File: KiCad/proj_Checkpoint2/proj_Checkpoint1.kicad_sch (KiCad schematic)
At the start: 32 parts, among them M1 Motor_Servo, Q2 MOSFET-N, SW1 Reset, U1 74xxx244, U1 MCP6294, U1 PIC32MX170F256B, U2 Comparator, U5 SW_CapTouch, U8 LED_Matrix

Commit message: clean build
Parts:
- added D4, D5, D6: LED, symbol Device:LED
- added R10, R12: 10k, symbol ME218_BaseLib:Res1
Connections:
- net GNDREF: now also D4.1 (K), D5.1 (K), D6.1 (K); no longer R1.2
- net out: now also U1.17 (5VT/RB8), U1.18 (PGED2/5VT/RB9), U1.24 (RB13)
- net at RV1.2: now also U1.26 (RB15); no longer U1.11 (RB4)
- net at D3.1 (K): no longer D2.2 (A)
- net at D3.2 (A): no longer U1.9 (RA2)
- net at R1.1: now also U1.21 (PGEC2/5VT/RB10); no longer D2.1 (K)
- net at U1.22 (RB11): now also R10.1
- net at U1.23 (RB12): now also R12.1
- new net: D6.2 (A), R12.2
- new net: D4.2 (A), R1.2
- new net: D5.2 (A), R10.2

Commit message: kicad update
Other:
- note added: "Coin Detector IR"
- note added: "Goal Sensor IR"
- note added: "Miss Sensor"
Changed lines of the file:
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@@
+    (stroke (width 0) (type default))
+  )
+  (wire (pts (xy 80.01 121.92) (xy 78.74 121.92))
+    (stroke (width 0) (type default))
+  )
+  (wire (pts (xy 154.94 96.52) (xy 154.94 99.06))
+    (stroke (width 0) (type default))
+  )
+  (wire (pts (xy 132.08 110.49) (xy 140.97 110.49))
+    (stroke (width 0) (type default))
+  )
+  (wire (pts (xy 134.62 182.88) (xy 138.43 182.88))
     (stroke (width 0) (type default))
   )
   (wire (pts (xy 132.08 130.81) (xy 137.16 130.81))
-    (stroke (width 0) (type default))
-  )
-  (wire (pts (xy 80.01 121.92) (xy 78.74 121.92))
-    (stroke (width 0) (type default))
-  )
-  (wire (pts (xy 154.94 96.52) (xy 154.94 99.06))
-    (stroke (width 0) (type default))
-  )
-  (wire (pts (xy 132.08 110.49) (xy 140.97 110.49))
-    (stroke (width 0) (type default))
-  )
-  (wire (pts (xy 134.62 182.88) (xy 138.43 182.88))
     (stroke (width 0) (type default))
   )
@@
     (effects (font (size 1.27 1.27)) (justify left bottom))
   )
-  (text "IR Sensor Signal Regulator\n" (at 106.68 171.45 0)
+  (text "Coin Detector IR" (at 106.68 171.45 0)
     (effects (font (size 1.27 1.27)) (justify left bottom))
   )
-  (text "IR Sensor Signal Regulator\n" (at 106.68 189.23 0)
+  (text "Goal Sensor IR\n" (at 106.68 189.23 0)
     (effects (font (size 1.27 1.27)) (justify left bottom))
   )
@@
     (effects (font (size 1.27 1.27)) (justify left bottom))
   )
-  (text "IR Sensor Signal Regulator\n" (at 106.68 180.34 0)
+  (text "Miss Sensor" (at 106.68 180.34 0)
     (effects (font (size 1.27 1.27)) (justify left bottom))
   )

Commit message: Updated KiCAD for Checkpoint 2
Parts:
- removed D2: IR LED1, symbol ME218_BaseLib:LED
- removed D3: IR LED0, symbol ME218_BaseLib:LED
- removed IR_Sensor0, IR_Sensor1: Photo_NPN, symbol ME218_BaseLib:Photo_NPN
- removed R2, R3: 10k, symbol ME218_BaseLib:Res1
- removed R4, R5: 330k, symbol ME218_BaseLib:Res1
- removed R6, R7: 22k, symbol ME218_BaseLib:Res1
- removed R8: 100k, symbol ME218_BaseLib:Res1
- removed R_pull1: 3.3k, symbol ME218_BaseLib:Res1
- removed U1: MCP6294, symbol ME218_BaseLib:MCP6294
- removed U2: Comparator, symbol ME218_BaseLib:MCP6294
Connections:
- net out: no longer U1.4 (PGED1/RB0), U1.5 (PGEC1/RB1)
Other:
- note added: "Coin Detector IR Emitter-Detector"
- note added: "Goal Sensor IR Emitter-Detector"
- note added: "Miss Sensor IR Emitter-Detector"
- note removed: "Coin Detector IR"
- note removed: "Goal Sensor IR"
- note removed: "IR Sensor Signal Regulator"
- note removed: "IR Sensor0 Output"
- note removed: "IR Sensor1 Output"
- note removed: "Miss Sensor"
- note removed: "input"
- title: (none) -> Project Checkpoint 2
- moved on the sheet: C1, C2, C3, C4, M1, Q2, R_gate, SW1, U1, U5, U8

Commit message: kicad update for report
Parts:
- removed U5: SW_CapTouch, symbol ME218_BaseLib:SW_CapTouch
- added R2: Res1, symbol ME218_BaseLib:Res1
- added SW2: SW_Push, symbol ME218_BaseLib:SW_Push
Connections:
- net +3.3V: now also SW2.1
- net GNDREF: now also R2.1
- net out: now also U1.16 (5VT/RB7)
- net at U1.14 (PGED3/5VT/RB5): now also R2.2, SW2.2
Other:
- note added: "Ball Placement IR Emitter-Detector"

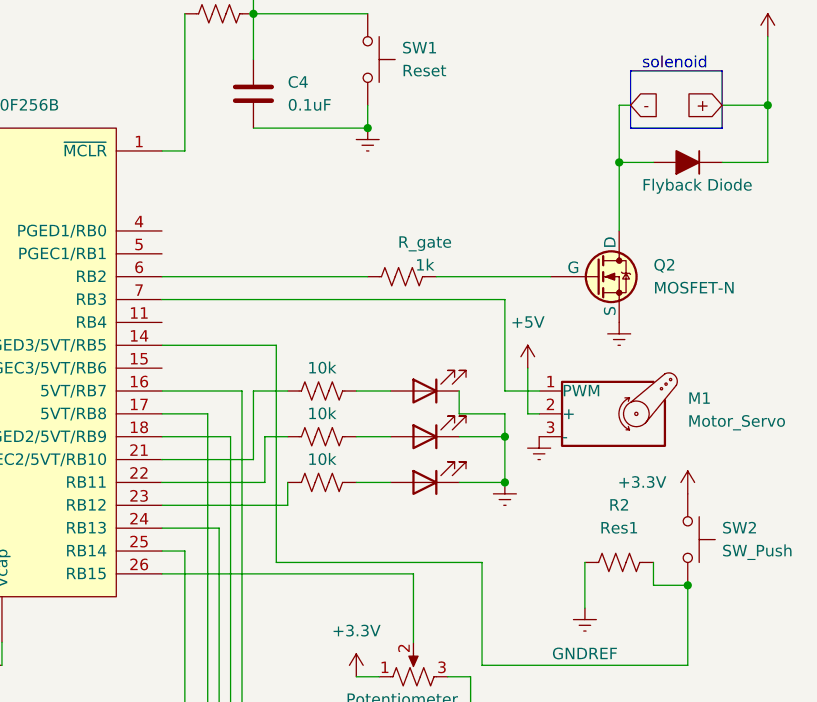
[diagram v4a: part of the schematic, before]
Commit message: added pull down resistor to mosfet
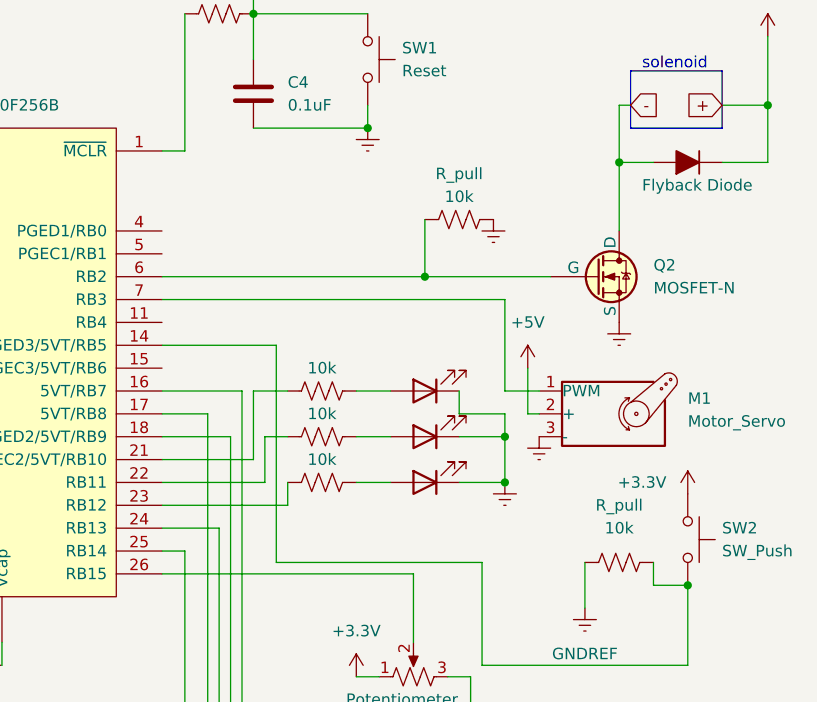
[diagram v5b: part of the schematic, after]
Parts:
- removed R_gate: 1k, symbol ME218_BaseLib:Res1
- added R_pull: 10k, symbol ME218_BaseLib:Res1
- R_pull: renamed from R2; value Res1 -> 10k
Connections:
- net GNDREF: now also R_pull.2
- net at U1.6 (RB2): now also Q2.2 (G), R_pull.1
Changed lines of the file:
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@@
 	)
 	(junction
+		(at 186.69 74.93)
+		(diameter 0)
+		(color 0 0 0 0)
+	)
+	(junction
 		(at 167.64 45.72)
 		(diameter 0)
@@
 	(wire
 		(pts
-			(xy 187.96 74.93) (xy 200.66 74.93)
+			(xy 186.69 74.93) (xy 200.66 74.93)
 		)
 		(stroke
@@
 	(wire
 		(pts
-			(xy 157.48 74.93) (xy 180.34 74.93)
+			(xy 157.48 74.93) (xy 186.69 74.93)
 		)
 		(stroke
@@
 	(wire
 		(pts
+			(xy 186.69 68.58) (xy 186.69 74.93)
+		)
+		(stroke
+			(width 0)
+			(type default)
+		)
+	)
+	(wire
+		(pts
 			(xy 168.91 97.79) (xy 157.48 97.79)
 		)
@@
 	)
 	(symbol
+		(lib_id "power:GNDREF")
+		(at 194.31 68.58 0)
+		(unit 1)
+		(exclude_from_sim no)
+		(in_bom yes)
+		(on_board yes)
+		(dnp no)
+		(fields_autoplaced yes)
+		(property "Reference" "#PWR05"
+			(at 194.31 74.93 0)
+			(effects
+				(font
+					(size 1.27 1.27)
+				)
+				(hide yes)
+			)
+		)
+		(property "Value" "GNDREF"
+			(at 194.31 73.66 0)
+			(effects
+				(font
+					(size 1.27 1.27)
+				)
+				(hide yes)
+			)
+		)
+		(property "Footprint" ""
+			(at 194.31 68.58 0)
+			(effects
+				(font
+					(size 1.27 1.27)
+				)
+				(hide yes)
+			)
+		)
+		(property "Datasheet" ""
+			(at 194.31 68.58 0)
+			(effects
+				(font
+					(size 1.27 1.27)
+				)
+				(hide yes)
+			)
+		)
+		(property "Description" ""
+			(at 194.31 68.58 0)
+			(effects
+				(font
+					(size 1.27 1.27)
+				)
+				(hide yes)
+			)
+		)
+		(pin "1"
+		)
+		(instances
+			(project "proj_Checkpoint1"
+				(path "/86ae32bf-6cc2-4ee9-9184-401e8238aa80"
+					(reference "#PWR05")
+					(unit 1)
+				)
+			)
+		)
+	)
+	(symbol
 		(lib_id "power:+5V")
 		(at 88.9 66.04 0)
@@
 		(dnp no)
 		(fields_autoplaced yes)
-		(property "Reference" "R2"
+		(property "Reference" "R_pull"
 			(at 208.28 100.33 90)
 			(effects
@@
 			)
 		)
-		(property "Value" "Res1"
+		(property "Value" "10k"
 			(at 208.28 102.87 90)
 			(effects
@@
 			(project "proj_Checkpoint1"
 				(path "/86ae32bf-6cc2-4ee9-9184-401e8238aa80"
-					(reference "R2")
+					(reference "R_pull")
 					(unit 1)
 				)
@@
 	)
 	(symbol
+		(lib_id "ME218_BaseLib:Res1")
+		(at 190.5 68.58 90)
+		(unit 1)
+		(exclude_from_sim no)
+		(in_bom yes)
+		(on_board yes)
+		(dnp no)
+		(property "Reference" "R_pull"
+			(at 190.5 63.5 90)
+			(effects
+				(font
+					(size 1.27 1.27)
+				)
+			)
+		)
+		(property "Value" "10k"
+			(at 190.5 66.04 90)
+			(effects
+				(font
+					(size 1.27 1.27)
+				)
+			)
+		)
+		(property "Footprint" ""
+			(at 190.754 67.564 90)
+			(effects
+				(font
+					(size 1.27 1.27)
+				)
+				(hide yes)
+			)
+		)
+		(property "Datasheet" ""
+			(at 190.5 68.58 0)
+			(effects
+				(font
+					(size 1.27 1.27)
+				)
+				(hide yes)
+			)
+		)
+		(property "Description" ""
+			(at 190.5 68.58 0)
+			(effects
+				(font
+					(size 1.27 1.27)
+				)
+				(hide yes)
+			)
+		)
+		(pin "1"
+		)
+		(pin "2"
+		)
+		(instances
+			(project "proj_Checkpoint1"
+				(path "/86ae32bf-6cc2-4ee9-9184-401e8238aa80"
+					(reference "R_pull")
+					(unit 1)
+				)
+			)
+		)
+	)
+	(symbol
 		(lib_id "power:GNDREF")
 		(at 109.22 72.39 0)
@@
 					(unit 1)
 				)
-			)
-		)
-	)
-	(symbol
-		(lib_id "ME218_BaseLib:Res1")
-		(at 184.15 74.93 90)
-		(unit 1)
-		(exclude_from_sim no)
-		(in_bom yes)
-		(on_board yes)
-		(dnp no)
-		(property "Reference" "R_gate"
-			(at 186.69 71.12 90)
-			(effects
-				(font
-					(size 1.27 1.27)
-				)
-			)
-		)
-		(property "Value" "1k"
-			(at 186.69 73.66 90)
-			(effects
-				(font
-					(size 1.27 1.27)
-				)
-			)
-		)
-		(property "Footprint" ""
-			(at 184.404 73.914 90)
-			(effects
-				(font
-					(size 1.27 1.27)
-				)
-				(hide yes)
-			)
-		)
-		(property "Datasheet" ""
-			(at 184.15 74.93 0)
-			(effects
-				(font
-					(size 1.27 1.27)
-				)
-				(hide yes)
-			)
-		)
-		(property "Description" ""
-			(at 184.15 74.93 0)
-			(effects
-				(font
-					(size 1.27 1.27)
-				)
-				(hide yes)
-			)
-		)
-		(pin "1"
-		)
-		(pin "2"
-		)
-		(instances
-			(project "proj_Checkpoint1"
-				(path "/86ae32bf-6cc2-4ee9-9184-401e8238aa80"
-					(reference "R_gate")
-					(unit 1)
-				)
